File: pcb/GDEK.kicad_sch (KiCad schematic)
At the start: 264 parts, among them J1 TYPE-C-31-M-13C, J101 TYPE-C-31-M-13C, J102 AudioJack3, J103 Debug pads, J2 AudioJack3, J3 Debug pads, SW1 SW_Push_45deg, SW10 SW_Push_45deg, SW101 SW_Push_45deg, SW102 SW_Push_45deg, SW103 SW_Push_45deg, SW104 SW_Push_45deg, SW105 SW_Push_45deg, SW106 SW_Push_45deg, SW107 SW_Push_45deg, SW108 SW_Push_45deg, SW109 SW_Push_45deg, SW11 SW_Push_45deg, SW110 SW_Push_45deg, SW111 SW_Push_45deg, SW112 SW_Push_45deg, SW113 SW_Push_45deg, SW114 SW_Push_45deg, SW115 SW_Push_45deg, SW116 SW_Push_45deg, SW117 SW_Push_45deg, SW118 SW_Push_45deg, SW119 SW_Push_45deg, SW12 SW_Push_45deg, SW120 SW_Push_45deg, SW121 SW_Push_45deg, SW122 SW_Push_45deg, SW123 SW_Push_45deg, SW124 SW_Push_45deg, SW125 SW_Push_45deg, SW126 SW_Push_45deg, SW127 SW_Push_45deg, SW128 SW_Push_45deg, SW129 SW_Push_45deg, SW13 SW_Push_45deg, SW130 SW_Push_45deg, SW131 RotaryEncoder_Switch, SW14 SW_Push_45deg, SW15 SW_Push_45deg, SW16 SW_Push_45deg, SW17 SW_Push_45deg, SW18 SW_Push_45deg, SW19 SW_Push_45deg, SW2 SW_Push_45deg, SW20 SW_Push_45deg, SW21 SW_Push_45deg, SW22 SW_Push_45deg, SW23 SW_Push_45deg, SW24 SW_Push_45deg, SW25 SW_Push_45deg, SW26 SW_Push_45deg, SW27 SW_Push_45deg, SW28 SW_Push_45deg, SW29 SW_Push_45deg, SW3 SW_Push_45deg, SW30 SW_Push_45deg, SW31 RotaryEncoder_Switch, SW4 SW_Push_45deg, SW5 SW_Push_45deg, SW6 SW_Push_45deg, SW7 SW_Push_45deg, SW8 SW_Push_45deg, SW9 SW_Push_45deg, U1 RP2040, U101 RP2040, U102 W25Q128JVP, U103 74AHCT1G125, U104 USBLC6-2P6, U105 XC6210B332MR, U2 W25Q128JVP, U3 74AHCT1G125, U4 USBLC6-2P6, U5 XC6210B332MR, Y1 ABM8-272-T3, Y101 ABM8-272-T3

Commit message: ♻️ Make switch symbol multi-unit for switch and LED
Also changes VBUS_PRESENCE voltage divider’s resistors and handedness pull-up/down resistor in order to remove one reference (10kΩ).
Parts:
- R10, R110: value 10kΩ -> 1kΩ; LCSC C25744 -> C11702
- R102, R2: value 10kΩ -> 5.1kΩ; LCSC C25744 -> C25905
- R11, R111: value 5.1kΩ -> 470Ω; LCSC C25905 -> C25117
- SW1: renamed from D31; footprint GDEK:SK6812MINIE -> GDEK:MX+KailhChoc+GateronKS+SK6812MINI-E_Tight; symbol LED:SK6812MINI -> GDEK:SW+SK6812MINIE
- SW1, SW10, SW101, SW102, SW103, SW104, SW105, SW106, SW107, SW108, SW109, SW11, SW110, SW111, SW112, SW113, SW114, SW115, SW116, SW117, SW118, SW119, SW12, SW120, SW121, SW122, SW123, SW124, SW125, SW126, SW127, SW128, SW129, SW13, SW130, SW14, SW15, SW16, SW17, SW18, SW19, SW2, SW20, SW21, SW22, SW23, SW24, SW25, SW26, SW27, SW28, SW29, SW3, SW30, SW4, SW5, SW6, SW7, SW8, SW9: value SW_Push_45deg -> SK6812MINI; footprint (none) -> GDEK:MX+KailhChoc+GateronKS+SK6812MINI-E_Tight; symbol Switch:SW_Push_45deg -> GDEK:SW+SK6812MINIE; LCSC (none) -> C5149201
- SW10: renamed from D40; footprint GDEK:SK6812MINIE -> GDEK:MX+KailhChoc+GateronKS+SK6812MINI-E_Tight; symbol LED:SK6812MINI -> GDEK:SW+SK6812MINIE
- SW101: renamed from D131; footprint GDEK:SK6812MINIE -> GDEK:MX+KailhChoc+GateronKS+SK6812MINI-E_Tight; symbol LED:SK6812MINI -> GDEK:SW+SK6812MINIE
- SW102: renamed from D132; footprint GDEK:SK6812MINIE -> GDEK:MX+KailhChoc+GateronKS+SK6812MINI-E_Tight; symbol LED:SK6812MINI -> GDEK:SW+SK6812MINIE
- SW103: renamed from D133; footprint GDEK:SK6812MINIE -> GDEK:MX+KailhChoc+GateronKS+SK6812MINI-E_Tight; symbol LED:SK6812MINI -> GDEK:SW+SK6812MINIE
- SW104: renamed from D134; footprint GDEK:SK6812MINIE -> GDEK:MX+KailhChoc+GateronKS+SK6812MINI-E_Tight; symbol LED:SK6812MINI -> GDEK:SW+SK6812MINIE
- SW105: renamed from D135; footprint GDEK:SK6812MINIE -> GDEK:MX+KailhChoc+GateronKS+SK6812MINI-E_Tight; symbol LED:SK6812MINI -> GDEK:SW+SK6812MINIE
- SW106: renamed from D136; footprint GDEK:SK6812MINIE -> GDEK:MX+KailhChoc+GateronKS+SK6812MINI-E_Tight; symbol LED:SK6812MINI -> GDEK:SW+SK6812MINIE
- SW107: renamed from D137; footprint GDEK:SK6812MINIE -> GDEK:MX+KailhChoc+GateronKS+SK6812MINI-E_Tight; symbol LED:SK6812MINI -> GDEK:SW+SK6812MINIE
- SW108: renamed from D138; footprint GDEK:SK6812MINIE -> GDEK:MX+KailhChoc+GateronKS+SK6812MINI-E_Tight; symbol LED:SK6812MINI -> GDEK:SW+SK6812MINIE
- SW109: renamed from D139; footprint GDEK:SK6812MINIE -> GDEK:MX+KailhChoc+GateronKS+SK6812MINI-E_Tight; symbol LED:SK6812MINI -> GDEK:SW+SK6812MINIE
- SW11: renamed from D41; footprint GDEK:SK6812MINIE -> GDEK:MX+KailhChoc+GateronKS+SK6812MINI-E_Tight; symbol LED:SK6812MINI -> GDEK:SW+SK6812MINIE
- SW110: renamed from D140; footprint GDEK:SK6812MINIE -> GDEK:MX+KailhChoc+GateronKS+SK6812MINI-E_Tight; symbol LED:SK6812MINI -> GDEK:SW+SK6812MINIE
- SW111: renamed from D141; footprint GDEK:SK6812MINIE -> GDEK:MX+KailhChoc+GateronKS+SK6812MINI-E_Tight; symbol LED:SK6812MINI -> GDEK:SW+SK6812MINIE
- SW112: renamed from D142; footprint GDEK:SK6812MINIE -> GDEK:MX+KailhChoc+GateronKS+SK6812MINI-E_Tight; symbol LED:SK6812MINI -> GDEK:SW+SK6812MINIE
- SW113: renamed from D143; footprint GDEK:SK6812MINIE -> GDEK:MX+KailhChoc+GateronKS+SK6812MINI-E_Tight; symbol LED:SK6812MINI -> GDEK:SW+SK6812MINIE
- SW114: renamed from D144; footprint GDEK:SK6812MINIE -> GDEK:MX+KailhChoc+GateronKS+SK6812MINI-E_Tight; symbol LED:SK6812MINI -> GDEK:SW+SK6812MINIE
- SW115: renamed from D145; footprint GDEK:SK6812MINIE -> GDEK:MX+KailhChoc+GateronKS+SK6812MINI-E_Tight; symbol LED:SK6812MINI -> GDEK:SW+SK6812MINIE
- SW116: renamed from D146; footprint GDEK:SK6812MINIE -> GDEK:MX+KailhChoc+GateronKS+SK6812MINI-E_Tight; symbol LED:SK6812MINI -> GDEK:SW+SK6812MINIE
- SW117: renamed from D147; footprint GDEK:SK6812MINIE -> GDEK:MX+KailhChoc+GateronKS+SK6812MINI-E_Tight; symbol LED:SK6812MINI -> GDEK:SW+SK6812MINIE
- SW118: renamed from D148; footprint GDEK:SK6812MINIE -> GDEK:MX+KailhChoc+GateronKS+SK6812MINI-E_Tight; symbol LED:SK6812MINI -> GDEK:SW+SK6812MINIE
- SW119: renamed from D149; footprint GDEK:SK6812MINIE -> GDEK:MX+KailhChoc+GateronKS+SK6812MINI-E_Tight; symbol LED:SK6812MINI -> GDEK:SW+SK6812MINIE
- SW12: renamed from D42; footprint GDEK:SK6812MINIE -> GDEK:MX+KailhChoc+GateronKS+SK6812MINI-E_Tight; symbol LED:SK6812MINI -> GDEK:SW+SK6812MINIE
- SW120: renamed from D150; footprint GDEK:SK6812MINIE -> GDEK:MX+KailhChoc+GateronKS+SK6812MINI-E_Tight; symbol LED:SK6812MINI -> GDEK:SW+SK6812MINIE
- SW121: renamed from D151; footprint GDEK:SK6812MINIE -> GDEK:MX+KailhChoc+GateronKS+SK6812MINI-E_Tight; symbol LED:SK6812MINI -> GDEK:SW+SK6812MINIE
- SW122: renamed from D152; footprint GDEK:SK6812MINIE -> GDEK:MX+KailhChoc+GateronKS+SK6812MINI-E_Tight; symbol LED:SK6812MINI -> GDEK:SW+SK6812MINIE
- SW123: renamed from D153; footprint GDEK:SK6812MINIE -> GDEK:MX+KailhChoc+GateronKS+SK6812MINI-E_Tight; symbol LED:SK6812MINI -> GDEK:SW+SK6812MINIE
- SW124: renamed from D154; footprint GDEK:SK6812MINIE -> GDEK:MX+KailhChoc+GateronKS+SK6812MINI-E_Tight; symbol LED:SK6812MINI -> GDEK:SW+SK6812MINIE
- SW125: renamed from D155; footprint GDEK:SK6812MINIE -> GDEK:MX+KailhChoc+GateronKS+SK6812MINI-E_Tight; symbol LED:SK6812MINI -> GDEK:SW+SK6812MINIE
- SW126: renamed from D156; footprint GDEK:SK6812MINIE -> GDEK:MX+KailhChoc+GateronKS+SK6812MINI-E_Tight; symbol LED:SK6812MINI -> GDEK:SW+SK6812MINIE
- SW127: renamed from D157; footprint GDEK:SK6812MINIE -> GDEK:MX+KailhChoc+GateronKS+SK6812MINI-E_Tight; symbol LED:SK6812MINI -> GDEK:SW+SK6812MINIE
- SW128: renamed from D158; footprint GDEK:SK6812MINIE -> GDEK:MX+KailhChoc+GateronKS+SK6812MINI-E_Tight; symbol LED:SK6812MINI -> GDEK:SW+SK6812MINIE
- SW129: renamed from D159; footprint GDEK:SK6812MINIE -> GDEK:MX+KailhChoc+GateronKS+SK6812MINI-E_Tight; symbol LED:SK6812MINI -> GDEK:SW+SK6812MINIE
- SW13: renamed from D43; footprint GDEK:SK6812MINIE -> GDEK:MX+KailhChoc+GateronKS+SK6812MINI-E_Tight; symbol LED:SK6812MINI -> GDEK:SW+SK6812MINIE
- SW130: renamed from D160; footprint GDEK:SK6812MINIE -> GDEK:MX+KailhChoc+GateronKS+SK6812MINI-E_Tight; symbol LED:SK6812MINI -> GDEK:SW+SK6812MINIE
- SW14: renamed from D44; footprint GDEK:SK6812MINIE -> GDEK:MX+KailhChoc+GateronKS+SK6812MINI-E_Tight; symbol LED:SK6812MINI -> GDEK:SW+SK6812MINIE
- SW15: renamed from D45; footprint GDEK:SK6812MINIE -> GDEK:MX+KailhChoc+GateronKS+SK6812MINI-E_Tight; symbol LED:SK6812MINI -> GDEK:SW+SK6812MINIE
- SW16: renamed from D46; footprint GDEK:SK6812MINIE -> GDEK:MX+KailhChoc+GateronKS+SK6812MINI-E_Tight; symbol LED:SK6812MINI -> GDEK:SW+SK6812MINIE
- SW17: renamed from D47; footprint GDEK:SK6812MINIE -> GDEK:MX+KailhChoc+GateronKS+SK6812MINI-E_Tight; symbol LED:SK6812MINI -> GDEK:SW+SK6812MINIE
- SW18: renamed from D48; footprint GDEK:SK6812MINIE -> GDEK:MX+KailhChoc+GateronKS+SK6812MINI-E_Tight; symbol LED:SK6812MINI -> GDEK:SW+SK6812MINIE
- SW19: renamed from D49; footprint GDEK:SK6812MINIE -> GDEK:MX+KailhChoc+GateronKS+SK6812MINI-E_Tight; symbol LED:SK6812MINI -> GDEK:SW+SK6812MINIE
- SW2: renamed from D32; footprint GDEK:SK6812MINIE -> GDEK:MX+KailhChoc+GateronKS+SK6812MINI-E_Tight; symbol LED:SK6812MINI -> GDEK:SW+SK6812MINIE
- SW20: renamed from D50; footprint GDEK:SK6812MINIE -> GDEK:MX+KailhChoc+GateronKS+SK6812MINI-E_Tight; symbol LED:SK6812MINI -> GDEK:SW+SK6812MINIE
- SW21: renamed from D51; footprint GDEK:SK6812MINIE -> GDEK:MX+KailhChoc+GateronKS+SK6812MINI-E_Tight; symbol LED:SK6812MINI -> GDEK:SW+SK6812MINIE
- SW22: renamed from D52; footprint GDEK:SK6812MINIE -> GDEK:MX+KailhChoc+GateronKS+SK6812MINI-E_Tight; symbol LED:SK6812MINI -> GDEK:SW+SK6812MINIE
- SW23: renamed from D53; footprint GDEK:SK6812MINIE -> GDEK:MX+KailhChoc+GateronKS+SK6812MINI-E_Tight; symbol LED:SK6812MINI -> GDEK:SW+SK6812MINIE
- SW24: renamed from D54; footprint GDEK:SK6812MINIE -> GDEK:MX+KailhChoc+GateronKS+SK6812MINI-E_Tight; symbol LED:SK6812MINI -> GDEK:SW+SK6812MINIE
- SW25: renamed from D55; footprint GDEK:SK6812MINIE -> GDEK:MX+KailhChoc+GateronKS+SK6812MINI-E_Tight; symbol LED:SK6812MINI -> GDEK:SW+SK6812MINIE
- SW26: renamed from D56; footprint GDEK:SK6812MINIE -> GDEK:MX+KailhChoc+GateronKS+SK6812MINI-E_Tight; symbol LED:SK6812MINI -> GDEK:SW+SK6812MINIE
- SW27: renamed from D57; footprint GDEK:SK6812MINIE -> GDEK:MX+KailhChoc+GateronKS+SK6812MINI-E_Tight; symbol LED:SK6812MINI -> GDEK:SW+SK6812MINIE
- SW28: renamed from D58; footprint GDEK:SK6812MINIE -> GDEK:MX+KailhChoc+GateronKS+SK6812MINI-E_Tight; symbol LED:SK6812MINI -> GDEK:SW+SK6812MINIE
- SW29: renamed from D59; footprint GDEK:SK6812MINIE -> GDEK:MX+KailhChoc+GateronKS+SK6812MINI-E_Tight; symbol LED:SK6812MINI -> GDEK:SW+SK6812MINIE
- SW3: renamed from D33; footprint GDEK:SK6812MINIE -> GDEK:MX+KailhChoc+GateronKS+SK6812MINI-E_Tight; symbol LED:SK6812MINI -> GDEK:SW+SK6812MINIE
- SW30: renamed from D60; footprint GDEK:SK6812MINIE -> GDEK:MX+KailhChoc+GateronKS+SK6812MINI-E_Tight; symbol LED:SK6812MINI -> GDEK:SW+SK6812MINIE
- SW4: renamed from D34; footprint GDEK:SK6812MINIE -> GDEK:MX+KailhChoc+GateronKS+SK6812MINI-E_Tight; symbol LED:SK6812MINI -> GDEK:SW+SK6812MINIE
- SW5: renamed from D35; footprint GDEK:SK6812MINIE -> GDEK:MX+KailhChoc+GateronKS+SK6812MINI-E_Tight; symbol LED:SK6812MINI -> GDEK:SW+SK6812MINIE
- SW6: renamed from D36; footprint GDEK:SK6812MINIE -> GDEK:MX+KailhChoc+GateronKS+SK6812MINI-E_Tight; symbol LED:SK6812MINI -> GDEK:SW+SK6812MINIE
- SW7: renamed from D37; footprint GDEK:SK6812MINIE -> GDEK:MX+KailhChoc+GateronKS+SK6812MINI-E_Tight; symbol LED:SK6812MINI -> GDEK:SW+SK6812MINIE
- SW8: renamed from D38; footprint GDEK:SK6812MINIE -> GDEK:MX+KailhChoc+GateronKS+SK6812MINI-E_Tight; symbol LED:SK6812MINI -> GDEK:SW+SK6812MINIE
- SW9: renamed from D39; footprint GDEK:SK6812MINIE -> GDEK:MX+KailhChoc+GateronKS+SK6812MINI-E_Tight; symbol LED:SK6812MINI -> GDEK:SW+SK6812MINIE
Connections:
- net +5V: now also SW1.3 (VDD), SW10.3 (VDD), SW11.3 (VDD), SW12.3 (VDD), SW13.3 (VDD), SW14.3 (VDD), SW15.3 (VDD), SW16.3 (VDD), SW17.3 (VDD), SW18.3 (VDD), SW19.3 (VDD), SW2.3 (VDD), SW20.3 (VDD), SW21.3 (VDD), SW22.3 (VDD), SW23.3 (VDD), SW24.3 (VDD), SW25.3 (VDD), SW26.3 (VDD), SW27.3 (VDD), SW28.3 (VDD), SW29.3 (VDD), SW3.3 (VDD), SW30.3 (VDD), SW4.3 (VDD), SW5.3 (VDD), SW6.3 (VDD), SW7.3 (VDD), SW8.3 (VDD), SW9.3 (VDD); no longer SW1.4 (VDD), SW10.4 (VDD), SW11.4 (VDD), SW12.4 (VDD), SW13.4 (VDD), SW14.4 (VDD), SW15.4 (VDD), SW16.4 (VDD), SW17.4 (VDD), SW18.4 (VDD), SW19.4 (VDD), SW2.4 (VDD), SW20.4 (VDD), SW21.4 (VDD), SW22.4 (VDD), SW23.4 (VDD), SW24.4 (VDD), SW25.4 (VDD), SW26.4 (VDD), SW27.4 (VDD), SW28.4 (VDD), SW29.4 (VDD), SW3.4 (VDD), SW30.4 (VDD), SW4.4 (VDD), SW5.4 (VDD), SW6.4 (VDD), SW7.4 (VDD), SW8.4 (VDD), SW9.4 (VDD)
- net +5V_R: now also SW101.3 (VDD), SW102.3 (VDD), SW103.3 (VDD), SW104.3 (VDD), SW105.3 (VDD), SW106.3 (VDD), SW107.3 (VDD), SW108.3 (VDD), SW109.3 (VDD), SW110.3 (VDD), SW111.3 (VDD), SW112.3 (VDD), SW113.3 (VDD), SW114.3 (VDD), SW115.3 (VDD), SW116.3 (VDD), SW117.3 (VDD), SW118.3 (VDD), SW119.3 (VDD), SW120.3 (VDD), SW121.3 (VDD), SW122.3 (VDD), SW123.3 (VDD), SW124.3 (VDD), SW125.3 (VDD), SW126.3 (VDD), SW127.3 (VDD), SW128.3 (VDD), SW129.3 (VDD), SW130.3 (VDD); no longer SW101.4 (VDD), SW102.4 (VDD), SW103.4 (VDD), SW104.4 (VDD), SW105.4 (VDD), SW106.4 (VDD), SW107.4 (VDD), SW108.4 (VDD), SW109.4 (VDD), SW110.4 (VDD), SW111.4 (VDD), SW112.4 (VDD), SW113.4 (VDD), SW114.4 (VDD), SW115.4 (VDD), SW116.4 (VDD), SW117.4 (VDD), SW118.4 (VDD), SW119.4 (VDD), SW120.4 (VDD), SW121.4 (VDD), SW122.4 (VDD), SW123.4 (VDD), SW124.4 (VDD), SW125.4 (VDD), SW126.4 (VDD), SW127.4 (VDD), SW128.4 (VDD), SW129.4 (VDD), SW130.4 (VDD)
- net COL0: now also SW1.5, SW13.5, SW19.5, SW25.5, SW7.5; no longer SW1.1, SW13.1, SW19.1, SW25.1, SW7.1
- net COL0_R: now also SW101.5, SW107.5, SW113.5, SW119.5, SW125.5; no longer SW101.1, SW107.1, SW113.1, SW119.1, SW125.1
- net COL1: now also SW14.5, SW2.5, SW20.5, SW26.5, SW8.5; no longer SW14.1, SW2.1, SW20.1, SW26.1, SW8.1
- net COL1_R: now also SW102.5, SW108.5, SW114.5, SW120.5, SW126.5; no longer SW102.1, SW108.1, SW114.1, SW120.1, SW126.1
- net COL2: now also SW15.5, SW21.5, SW27.5, SW3.5, SW9.5; no longer SW15.1, SW21.1, SW27.1, SW3.1, SW9.1
- net COL2_R: now also SW103.5, SW109.5, SW115.5, SW121.5, SW127.5; no longer SW103.1, SW109.1, SW115.1, SW121.1, SW127.1
- net COL3: now also SW10.5, SW16.5, SW22.5, SW28.5, SW4.5; no longer SW10.1, SW16.1, SW22.1, SW28.1, SW4.1
- net COL3_R: now also SW104.5, SW110.5, SW116.5, SW122.5, SW128.5; no longer SW104.1, SW110.1, SW116.1, SW122.1, SW128.1
- net COL4: now also SW11.5, SW17.5, SW23.5, SW29.5, SW5.5; no longer SW11.1, SW17.1, SW23.1, SW29.1, SW5.1
- net COL4_R: now also SW105.5, SW111.5, SW117.5, SW123.5, SW129.5; no longer SW105.1, SW111.1, SW117.1, SW123.1, SW129.1
- net COL5: now also SW12.5, SW18.5, SW24.5, SW30.5, SW6.5; no longer SW12.1, SW18.1, SW24.1, SW30.1, SW6.1
- net COL5_R: now also SW106.5, SW112.5, SW118.5, SW124.5, SW130.5; no longer SW106.1, SW112.1, SW118.1, SW124.1, SW130.1
- net GND: now also SW1.1 (VSS), SW10.1 (VSS), SW11.1 (VSS), SW12.1 (VSS), SW13.1 (VSS), SW14.1 (VSS), SW15.1 (VSS), SW16.1 (VSS), SW17.1 (VSS), SW18.1 (VSS), SW19.1 (VSS), SW2.1 (VSS), SW20.1 (VSS), SW21.1 (VSS), SW22.1 (VSS), SW23.1 (VSS), SW24.1 (VSS), SW25.1 (VSS), SW26.1 (VSS), SW27.1 (VSS), SW28.1 (VSS), SW29.1 (VSS), SW3.1 (VSS), SW30.1 (VSS), SW4.1 (VSS), SW5.1 (VSS), SW6.1 (VSS), SW7.1 (VSS), SW8.1 (VSS), SW9.1 (VSS); no longer SW1.2 (VSS), SW10.2 (VSS), SW11.2 (VSS), SW12.2 (VSS), SW13.2 (VSS), SW14.2 (VSS), SW15.2 (VSS), SW16.2 (VSS), SW17.2 (VSS), SW18.2 (VSS), SW19.2 (VSS), SW2.2 (VSS), SW20.2 (VSS), SW21.2 (VSS), SW22.2 (VSS), SW23.2 (VSS), SW24.2 (VSS), SW25.2 (VSS), SW26.2 (VSS), SW27.2 (VSS), SW28.2 (VSS), SW29.2 (VSS), SW3.2 (VSS), SW30.2 (VSS), SW4.2 (VSS), SW5.2 (VSS), SW6.2 (VSS), SW7.2 (VSS), SW8.2 (VSS), SW9.2 (VSS)
- net GND_R: now also SW101.1 (VSS), SW102.1 (VSS), SW103.1 (VSS), SW104.1 (VSS), SW105.1 (VSS), SW106.1 (VSS), SW107.1 (VSS), SW108.1 (VSS), SW109.1 (VSS), SW110.1 (VSS), SW111.1 (VSS), SW112.1 (VSS), SW113.1 (VSS), SW114.1 (VSS), SW115.1 (VSS), SW116.1 (VSS), SW117.1 (VSS), SW118.1 (VSS), SW119.1 (VSS), SW120.1 (VSS), SW121.1 (VSS), SW122.1 (VSS), SW123.1 (VSS), SW124.1 (VSS), SW125.1 (VSS), SW126.1 (VSS), SW127.1 (VSS), SW128.1 (VSS), SW129.1 (VSS), SW130.1 (VSS); no longer SW101.2 (VSS), SW102.2 (VSS), SW103.2 (VSS), SW104.2 (VSS), SW105.2 (VSS), SW106.2 (VSS), SW107.2 (VSS), SW108.2 (VSS), SW109.2 (VSS), SW110.2 (VSS), SW111.2 (VSS), SW112.2 (VSS), SW113.2 (VSS), SW114.2 (VSS), SW115.2 (VSS), SW116.2 (VSS), SW117.2 (VSS), SW118.2 (VSS), SW119.2 (VSS), SW120.2 (VSS), SW121.2 (VSS), SW122.2 (VSS), SW123.2 (VSS), SW124.2 (VSS), SW125.2 (VSS), SW126.2 (VSS), SW127.2 (VSS), SW128.2 (VSS), SW129.2 (VSS), SW130.2 (VSS)
- net at D30.2 (A): now also SW30.6; no longer SW30.2
- net at D120.2 (A): now also SW120.6; no longer SW120.2
- net at D17.2 (A): now also SW17.6; no longer SW17.2
- net at D110.2 (A): now also SW110.6; no longer SW110.2
- net at D121.2 (A): now also SW121.6; no longer SW121.2
- net at D29.2 (A): now also SW29.6; no longer SW29.2
- net at D10.2 (A): now also SW10.6; no longer SW10.2
- net at D128.2 (A): now also SW128.6; no longer SW128.2
- net at D16.2 (A): now also SW16.6; no longer SW16.2
- net at D126.2 (A): now also SW126.6; no longer SW126.2
- net at U103.4: now also SW101.2 (DIN); no longer SW101.3 (DIN)
- net at D14.2 (A): now also SW14.6; no longer SW14.2
- net at D23.2 (A): now also SW23.6; no longer SW23.2
- net at D9.2 (A): now also SW9.6; no longer SW9.2
- net at D25.2 (A): now also SW25.6; no longer SW25.2
- net at D115.2 (A): now also SW115.6; no longer SW115.2
- net at D4.2 (A): now also SW4.6; no longer SW4.2
- net at D124.2 (A): now also SW124.6; no longer SW124.2
- net at D20.2 (A): now also SW20.6; no longer SW20.2
- net at D7.2 (A): now also SW7.6; no longer SW7.2
- net at D22.2 (A): now also SW22.6; no longer SW22.2
- net at D18.2 (A): now also SW18.6; no longer SW18.2
- net at D101.2 (A): now also SW101.6; no longer SW101.2
- net at D15.2 (A): now also SW15.6; no longer SW15.2
- net at D2.2 (A): now also SW2.6; no longer SW2.2
- net at D109.2 (A): now also SW109.6; no longer SW109.2
- net at D127.2 (A): now also SW127.6; no longer SW127.2
- net at D13.2 (A): now also SW13.6; no longer SW13.2
- net at D26.2 (A): now also SW26.6; no longer SW26.2
- net at D21.2 (A): now also SW21.6; no longer SW21.2
- net at D106.2 (A): now also SW106.6; no longer SW106.2
- net at D122.2 (A): now also SW122.6; no longer SW122.2
- net at D3.2 (A): now also SW3.6; no longer SW3.2
- net at D117.2 (A): now also SW117.6; no longer SW117.2
- net at D130.2 (A): now also SW130.6; no longer SW130.2
- net at D107.2 (A): now also SW107.6; no longer SW107.2
- net at D119.2 (A): now also SW119.6; no longer SW119.2
- net at D28.2 (A): now also SW28.6; no longer SW28.2
- net at D8.2 (A): now also SW8.6; no longer SW8.2
- net at D11.2 (A): now also SW11.6; no longer SW11.2
- net at D5.2 (A): now also SW5.6; no longer SW5.2
- net at D102.2 (A): now also SW102.6; no longer SW102.2
- net at D24.2 (A): now also SW24.6; no longer SW24.2
- net at D118.2 (A): now also SW118.6; no longer SW118.2
- net at D104.2 (A): now also SW104.6; no longer SW104.2
- net at D129.2 (A): now also SW129.6; no longer SW129.2
- net at D12.2 (A): now also SW12.6; no longer SW12.2
- net at D6.2 (A): now also SW6.6; no longer SW6.2
- net at U3.4: now also SW1.2 (DIN); no longer SW1.3 (DIN)
- net at D108.2 (A): now also SW108.6; no longer SW108.2
- net at D27.2 (A): now also SW27.6; no longer SW27.2
- net at D103.2 (A): now also SW103.6; no longer SW103.2
- net at D123.2 (A): now also SW123.6; no longer SW123.2
- net at D1.2 (A): now also SW1.6; no longer SW1.2
- net at D113.2 (A): now also SW113.6; no longer SW113.2
- net at D114.2 (A): now also SW114.6; no longer SW114.2
- net at D19.2 (A): now also SW19.6; no longer SW19.2
- net at D105.2 (A): now also SW105.6; no longer SW105.2
- net at D125.2 (A): now also SW125.6; no longer SW125.2
- net at D111.2 (A): now also SW111.6; no longer SW111.2
- net at D116.2 (A): now also SW116.6; no longer SW116.2
- net at D112.2 (A): now also SW112.6; no longer SW112.2
- new net: SW101.4 (DOUT), SW102.2 (DIN)
- new net: SW102.4 (DOUT), SW103.2 (DIN)
- new net: SW16.4 (DOUT), SW17.2 (DIN)
- new net: SW17.4 (DOUT), SW18.2 (DIN)
- new net: SW25.4 (DOUT), SW26.2 (DIN)
- new net: SW26.4 (DOUT), SW27.2 (DIN)
- new net: SW117.4 (DOUT), SW118.2 (DIN)
- new net: SW118.4 (DOUT), SW119.2 (DIN)
- new net: SW27.4 (DOUT), SW28.2 (DIN)
- new net: SW28.4 (DOUT), SW29.2 (DIN)
- new net: SW106.4 (DOUT), SW107.2 (DIN)
- new net: SW107.4 (DOUT), SW108.2 (DIN)
- new net: SW18.4 (DOUT), SW19.2 (DIN)
- new net: SW22.4 (DOUT), SW23.2 (DIN)
- new net: SW23.4 (DOUT), SW24.2 (DIN)
- new net: SW29.4 (DOUT), SW30.2 (DIN)
- new net: SW114.4 (DOUT), SW115.2 (DIN)
- new net: SW115.4 (DOUT), SW116.2 (DIN)
- new net: SW1.4 (DOUT), SW2.2 (DIN)
- new net: SW2.4 (DOUT), SW3.2 (DIN)
- new net: SW108.4 (DOUT), SW109.2 (DIN)
- new net: SW14.4 (DOUT), SW15.2 (DIN)
- new net: SW15.4 (DOUT), SW16.2 (DIN)
- new net: SW12.4 (DOUT), SW13.2 (DIN)
- new net: SW13.4 (DOUT), SW14.2 (DIN)
- new net: SW109.4 (DOUT), SW110.2 (DIN)
- new net: SW110.4 (DOUT), SW111.2 (DIN)
- new net: SW113.4 (DOUT), SW114.2 (DIN)
- new net: SW4.4 (DOUT), SW5.2 (DIN)
- new net: SW5.4 (DOUT), SW6.2 (DIN)
- new net: SW24.4 (DOUT), SW25.2 (DIN)
- new net: SW19.4 (DOUT), SW20.2 (DIN)
- new net: SW20.4 (DOUT), SW21.2 (DIN)
- new net: SW3.4 (DOUT), SW4.2 (DIN)
- new net: SW123.4 (DOUT), SW124.2 (DIN)
- new net: SW124.4 (DOUT), SW125.2 (DIN)
- new net: SW103.4 (DOUT), SW104.2 (DIN)
- new net: SW104.4 (DOUT), SW105.2 (DIN)
- new net: SW119.4 (DOUT), SW120.2 (DIN)
- new net: SW120.4 (DOUT), SW121.2 (DIN)
- new net: SW11.4 (DOUT), SW12.2 (DIN)
- new net: SW125.4 (DOUT), SW126.2 (DIN)
- new net: SW126.4 (DOUT), SW127.2 (DIN)
- new net: SW129.4 (DOUT), SW130.2 (DIN)
- new net: SW116.4 (DOUT), SW117.2 (DIN)
- new net: SW21.4 (DOUT), SW22.2 (DIN)
- new net: SW122.4 (DOUT), SW123.2 (DIN)
- new net: SW7.4 (DOUT), SW8.2 (DIN)
- new net: SW8.4 (DOUT), SW9.2 (DIN)
- new net: SW111.4 (DOUT), SW112.2 (DIN)
- new net: SW127.4 (DOUT), SW128.2 (DIN)
- new net: SW121.4 (DOUT), SW122.2 (DIN)
- new net: SW112.4 (DOUT), SW113.2 (DIN)
- new net: SW10.2 (DIN), SW9.4 (DOUT)
- new net: SW10.4 (DOUT), SW11.2 (DIN)
- new net: SW128.4 (DOUT), SW129.2 (DIN)
- new net: SW6.4 (DOUT), SW7.2 (DIN)
- new net: SW105.4 (DOUT), SW106.2 (DIN)

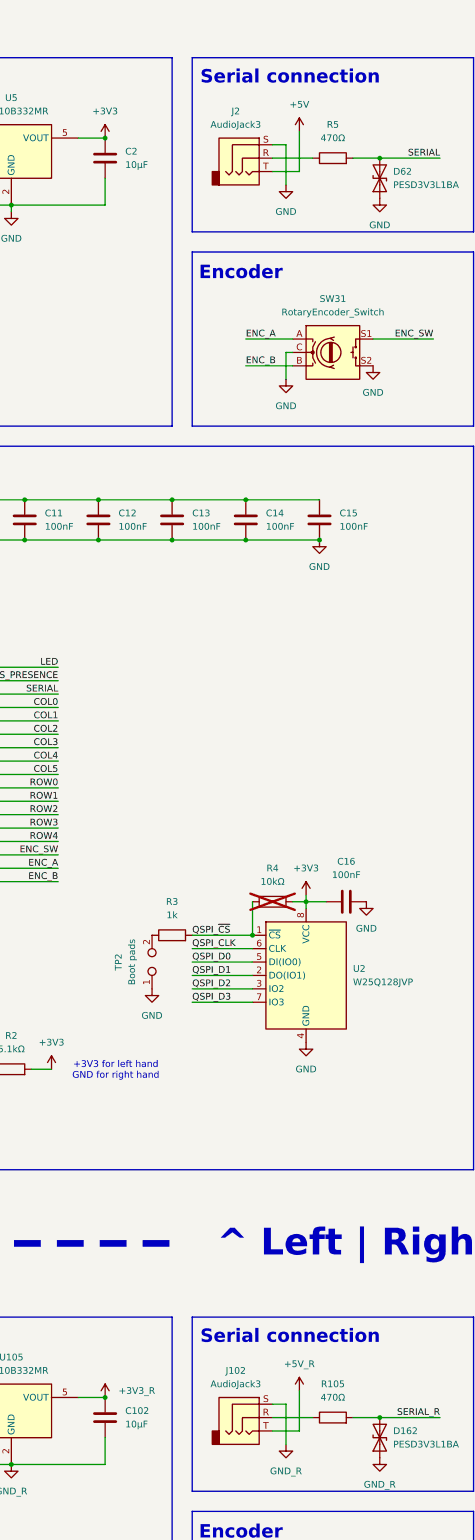
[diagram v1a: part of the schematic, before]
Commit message: 🔧 Finish footprint assignments
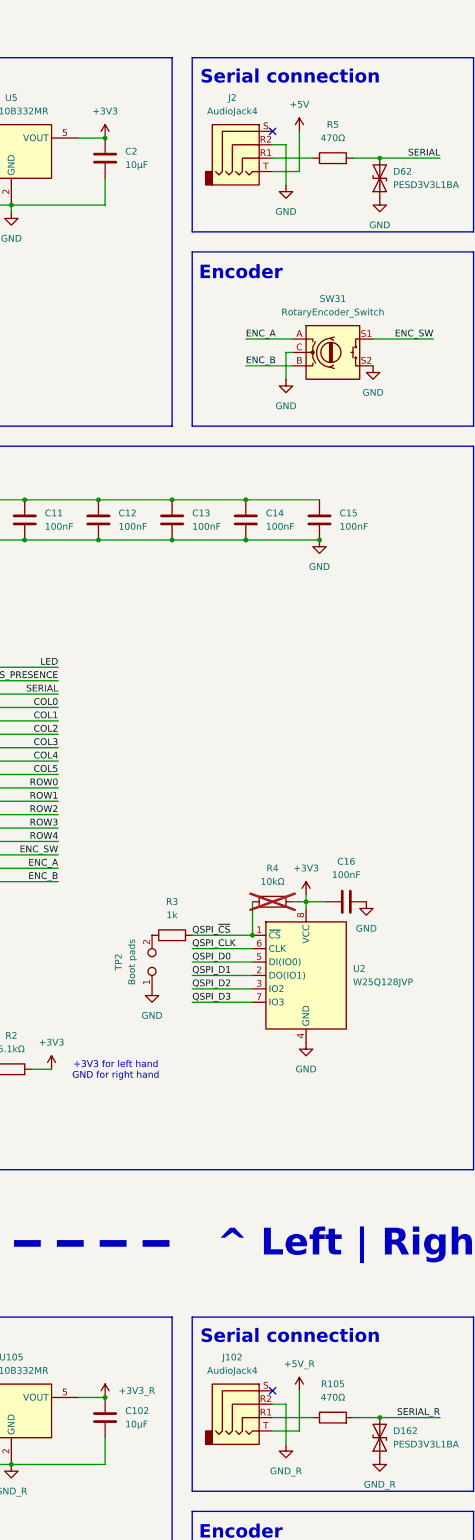
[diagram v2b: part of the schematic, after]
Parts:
- removed J102, J2: AudioJack3, symbol Connector_Audio:AudioJack3
- added J102, J2: AudioJack4, GDEK:AUDIO-TH_PJ-320A-4P-DIP, symbol Connector_Audio:AudioJack4
- SW131, SW31: footprint (none) -> Rotary_Encoder:RotaryEncoder_Alps_EC11E-Switch_Vertical_H20mm
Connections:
- net +5V: now also J2.T
- net +5V_R: now also J102.T
- net GND: now also J2.R2
- net GND_R: now also J102.R2
- net at R5.1: now also J2.R1
- net at R105.1: now also J102.R1
- no-connect marks 30 -> 32
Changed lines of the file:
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@@
 	)
 	(no_connect
+		(at 190.5 274.32)
+	)
+	(no_connect
 		(at 133.35 426.72)
 	)
@@
 	)
 	(no_connect
+		(at 190.5 35.56)
+	)
+	(no_connect
 		(at 133.35 200.66)
 	)
@@
 			)
 		)
-		(property "Footprint" ""
+		(property "Footprint" "Rotary_Encoder:RotaryEncoder_Alps_EC11E-Switch_Vertical_H20mm"
 			(at 198.12 73.406 0)
 			(effects
@@
 	)
 	(symbol
-		(lib_id "Connector_Audio:AudioJack3")
-		(at 185.42 279.4 0)
-		(unit 1)
-		(exclude_from_sim no)
-		(in_bom yes)
-		(on_board yes)
-		(dnp no)
-		(fields_autoplaced yes)
-		(property "Reference" "J102"
-			(at 183.515 270.51 0)
-			(effects
-				(font
-					(size 1.27 1.27)
-				)
-			)
-		)
-		(property "Value" "AudioJack3"
-			(at 183.515 273.05 0)
-			(effects
-				(font
-					(size 1.27 1.27)
-				)
-			)
-		)
-		(property "Footprint" ""
-			(at 185.42 279.4 0)
-			(effects
-				(font
-					(size 1.27 1.27)
-				)
-				(hide yes)
-			)
-		)
-		(property "Datasheet" "~"
-			(at 185.42 279.4 0)
-			(effects
-				(font
-					(size 1.27 1.27)
-				)
-				(hide yes)
-			)
-		)
-		(property "Description" "Audio Jack, 3 Poles (Stereo / TRS)"
-			(at 185.42 279.4 0)
-			(effects
-				(font
-					(size 1.27 1.27)
-				)
-				(hide yes)
-			)
-		)
-		(pin "S"
-		)
-		(pin "T"
-		)
-		(pin "R"
-		)
-		(instances
-			(project "GDEK"
-				(path "/c27e6219-942d-4ad4-b4df-18894276b69d"
-					(reference "J102")
-					(unit 1)
-				)
-			)
-		)
-	)
-	(symbol
 		(lib_id "power:PWR_FLAG")
 		(at -20.32 34.29 180)
@@
 			)
 		)
-		(property "Footprint" ""
+		(property "Footprint" "Rotary_Encoder:RotaryEncoder_Alps_EC11E-Switch_Vertical_H20mm"
 			(at 198.12 312.166 0)
 			(effects
@@
 	)
 	(symbol
+		(lib_id "Connector_Audio:AudioJack4")
+		(at 185.42 276.86 0)
+		(unit 1)
+		(exclude_from_sim no)
+		(in_bom yes)
+		(on_board yes)
+		(dnp no)
+		(fields_autoplaced yes)
+		(property "Reference" "J102"
+			(at 182.88 267.97 0)
+			(effects
+				(font
+					(size 1.27 1.27)
+				)
+			)
+		)
+		(property "Value" "AudioJack4"
+			(at 182.88 270.51 0)
+			(effects
+				(font
+					(size 1.27 1.27)
+				)
+			)
+		)
+		(property "Footprint" "GDEK:AUDIO-TH_PJ-320A-4P-DIP"
+			(at 185.42 276.86 0)
+			(effects
+				(font
+					(size 1.27 1.27)
+				)
+				(hide yes)
+			)
+		)
+		(property "Datasheet" "~"
+			(at 185.42 276.86 0)
+			(effects
+				(font
+					(size 1.27 1.27)
+				)
+				(hide yes)
+			)
+		)
+		(property "Description" "Audio Jack, 4 Poles (TRRS)"
+			(at 185.42 276.86 0)
+			(effects
+				(font
+					(size 1.27 1.27)
+				)
+				(hide yes)
+			)
+		)
+		(property "LCSC" "C18185602"
+			(at 185.42 276.86 0)
+			(effects
+				(font
+					(size 1.27 1.27)
+				)
+				(hide yes)
+			)
+		)
+		(pin "S"
+		)
+		(pin "R1"
+		)
+		(pin "R2"
+		)
+		(pin "T"
+		)
+		(instances
+			(project "GDEK"
+				(path "/c27e6219-942d-4ad4-b4df-18894276b69d"
+					(reference "J102")
+					(unit 1)
+				)
+			)
+		)
+	)
+	(symbol
 		(lib_id "Power_Protection:USBLC6-2P6")
 		(at 81.28 311.15 0)
@@
 	)
 	(symbol
+		(lib_id "Connector_Audio:AudioJack4")
+		(at 185.42 38.1 0)
+		(unit 1)
+		(exclude_from_sim no)
+		(in_bom yes)
+		(on_board yes)
+		(dnp no)
+		(fields_autoplaced yes)
+		(property "Reference" "J2"
+			(at 182.88 29.21 0)
+			(effects
+				(font
+					(size 1.27 1.27)
+				)
+			)
+		)
+		(property "Value" "AudioJack4"
+			(at 182.88 31.75 0)
+			(effects
+				(font
+					(size 1.27 1.27)
+				)
+			)
+		)
+		(property "Footprint" "GDEK:AUDIO-TH_PJ-320A-4P-DIP"
+			(at 185.42 38.1 0)
+			(effects
+				(font
+					(size 1.27 1.27)
+				)
+				(hide yes)
+			)
+		)
+		(property "Datasheet" "~"
+			(at 185.42 38.1 0)
+			(effects
+				(font
+					(size 1.27 1.27)
+				)
+				(hide yes)
+			)
+		)
+		(property "Description" "Audio Jack, 4 Poles (TRRS)"
+			(at 185.42 38.1 0)
+			(effects
+				(font
+					(size 1.27 1.27)
+				)
+				(hide yes)
+			)
+		)
+		(property "LCSC" "C18185602"
+			(at 185.42 38.1 0)
+			(effects
+				(font
+					(size 1.27 1.27)
+				)
+				(hide yes)
+			)
+		)
+		(pin "S"
+		)
+		(pin "R1"
+		)
+		(pin "R2"
+		)
+		(pin "T"
+		)
+		(instances
+			(project ""
+				(path "/c27e6219-942d-4ad4-b4df-18894276b69d"
+					(reference "J2")
+					(unit 1)
+				)
+			)
+		)
+	)
+	(symbol
 		(lib_id "Device:R")
 		(at 78.74 386.08 90)
@@
 					(unit 1)
 				)
-			)
-		)
-	)
-	(symbol
-		(lib_id "Connector_Audio:AudioJack3")
-		(at 185.42 40.64 0)
-		(unit 1)
-		(exclude_from_sim no)
-		(in_bom yes)
-		(on_board yes)
-		(dnp no)
-		(fields_autoplaced yes)
-		(property "Reference" "J2"
-			(at 183.515 31.75 0)
-			(effects
-				(font
-					(size 1.27 1.27)
-				)
-			)
-		)
-		(property "Value" "AudioJack3"
-			(at 183.515 34.29 0)
-			(effects
-				(font
-					(size 1.27 1.27)
-				)
-			)
-		)
-		(property "Footprint" ""
-			(at 185.42 40.64 0)
-			(effects
-				(font
-					(size 1.27 1.27)
-				)
-				(hide yes)
-			)
-		)
-		(property "Datasheet" "~"
-			(at 185.42 40.64 0)
-			(effects
-				(font
-					(size 1.27 1.27)
-				)
-				(hide yes)
-			)
-		)
-		(property "Description" "Audio Jack, 3 Poles (Stereo / TRS)"
-			(at 185.42 40.64 0)
-			(effects
-				(font
-					(size 1.27 1.27)
-				)
-				(hide yes)
-			)
-		)
-		(pin "S"
-		)
-		(pin "T"
-		)
-		(pin "R"
-		)
-		(instances
-			(project ""
-				(path "/c27e6219-942d-4ad4-b4df-18894276b69d"
-					(reference "J2")
-					(unit 1)
-				)

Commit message: ✨ Finish left hand PCB
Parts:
- removed U102, U2: W25Q128JVP, Package_SON:WSON-8-1EP_6x5mm_P1.27mm_EP3.4x4.3mm, symbol Memory_Flash:W25Q128JVP
- added U102, U2: W25Q128JVS, Package_SO:SOIC-8_5.23x5.23mm_P1.27mm, symbol Memory_Flash:W25Q128JVS
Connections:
- net +3V3: now also U2.8 (VCC)
- net +3V3_R: now also U102.8 (VCC)
- net COL0: now also U1.39 (GPIO27_ADC1); no longer U1.5 (GPIO3)
- net COL1: now also U1.38 (GPIO26_ADC0); no longer U1.6 (GPIO4)
- net COL2: now also U1.37 (GPIO25); no longer U1.7 (GPIO5)
- net COL3: now also U1.36 (GPIO24); no longer U1.8 (GPIO6)
- net COL4: now also U1.35 (GPIO23); no longer U1.9 (GPIO7)
- net COL5: now also U1.34 (GPIO22); no longer U1.11 (GPIO8)
- net ENC_A: now also U1.17 (GPIO14); no longer U1.18 (GPIO15)
- net ENC_B: now also U1.18 (GPIO15); no longer U1.27 (GPIO16)
- net ENC_SW: now also U1.16 (GPIO13); no longer U1.17 (GPIO14)
- net GND: now also U2.4 (GND)
- net GND_R: now also U102.4 (GND)
- net LED: now also U1.41 (GPIO29_ADC3); no longer U1.2 (GPIO0)
- net QSPI_CLK: now also U2.6 (CLK)
- net QSPI_CLK_R: now also U102.6 (CLK)
- net QSPI_D0: now also U2.5 (DI(IO0))
- net QSPI_D0_R: now also U102.5 (DI(IO0))
- net QSPI_D1: now also U2.2 (DO(IO1))
- net QSPI_D1_R: now also U102.2 (DO(IO1))
- net QSPI_D2: now also U2.3 (IO2)
- net QSPI_D2_R: now also U102.3 (IO2)
- net QSPI_D3: now also U2.7 (IO3)
- net QSPI_D3_R: now also U102.7 (IO3)
- net QSPI_~{CS}: now also U2.1 (~{CS})
- net QSPI_~{CS}_R: now also U102.1 (~{CS})
- net ROW0: now also U1.40 (GPIO28_ADC2); no longer U1.12 (GPIO9)
- net ROW1: now also U1.32 (GPIO21); no longer U1.13 (GPIO10)
- net ROW2: now also U1.31 (GPIO20); no longer U1.14 (GPIO11)
- net ROW3: now also U1.30 (GPIO19); no longer U1.15 (GPIO12)
- net ROW4: now also U1.29 (GPIO18); no longer U1.16 (GPIO13)
- net SERIAL: now also U1.3 (GPIO1); no longer U1.4 (GPIO2)
- net VBUS_PRESENCE: now also U1.2 (GPIO0); no longer U1.3 (GPIO1)
- net at SW17.2 (DIN): now also SW18.4 (DOUT); no longer SW16.4 (DOUT)
- net at SW17.4 (DOUT): now also SW16.2 (DIN); no longer SW18.2 (DIN)
- net at SW26.2 (DIN): now also SW27.4 (DOUT); no longer SW25.4 (DOUT)
- net at SW26.4 (DOUT): now also SW25.2 (DIN); no longer SW27.2 (DIN)
- net at SW28.2 (DIN): now also SW29.4 (DOUT); no longer SW27.4 (DOUT)
- net at SW28.4 (DOUT): now also SW27.2 (DIN); no longer SW29.2 (DIN)
- net at SW19.2 (DIN): now also SW13.4 (DOUT); no longer SW18.4 (DOUT)
- net at SW30.2 (DIN): now also SW24.4 (DOUT); no longer SW29.4 (DOUT)
- net at SW2.2 (DIN): now also SW3.4 (DOUT); no longer SW1.4 (DOUT)
- net at SW2.4 (DOUT): now also SW1.2 (DIN); no longer SW3.2 (DIN)
- net at SW30.4 (DOUT): now also SW29.2 (DIN)
- net at SW15.2 (DIN): now also SW16.4 (DOUT); no longer SW14.4 (DOUT)
- net at SW15.4 (DOUT): now also SW14.2 (DIN); no longer SW16.2 (DIN)
- net at SW12.4 (DOUT): now also SW18.2 (DIN); no longer SW13.2 (DIN)
- net at SW5.2 (DIN): now also SW6.4 (DOUT); no longer SW4.4 (DOUT)
- net at SW5.4 (DOUT): now also SW4.2 (DIN); no longer SW6.2 (DIN)
- net at R2.1: now also U1.15 (GPIO12); no longer U1.41 (GPIO29_ADC3)
- net at U3.4: now also SW6.2 (DIN); no longer SW1.2 (DIN)
- net at SW7.2 (DIN): now also SW1.4 (DOUT); no longer SW6.4 (DOUT)
- new net: SW13.2 (DIN), SW14.4 (DOUT)
- new net: SW3.2 (DIN), SW4.4 (DOUT)
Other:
- moved on the sheet: F1, R2, R8, R9, SW13B, SW14B, SW15B, SW16B, SW17B, SW18B, SW1B, SW25B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

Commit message: ✨ Add optional decoupling for each LED
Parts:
- added C117, C118, C119, C120, C121, C122, C123, C124, C125, C126, C127, C128, C129, C130, C131, C132, C133, C134, C135, C136, C137, C138, C139, C140, C141, C142, C143, C144, C145, C146, C147, C17, C18, C19, C20, C21, C22, C23, C24, C25, C26, C27, C28, C29, C30, C31, C32, C33, C34, C35, C36, C37, C38, C39, C40, C41, C42, C43, C44, C45, C46, C47: 100nF, Capacitor_SMD:C_0402_1005Metric, symbol Device:C
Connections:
- net +5V: now also C17.2, C18.2, C19.2, C20.2, C21.2, C22.2, C23.2, C24.2, C25.2, C26.2, C27.2, C28.2, C29.2, C30.2, C31.2, C32.2, C33.2, C34.2, C35.2, C36.2, C37.2, C38.2, C39.2, C40.2, C41.2, C42.2, C43.2, C44.2, C45.2, C46.2, C47.2
- net +5V_R: now also C117.2, C118.2, C119.2, C120.2, C121.2, C122.2, C123.2, C124.2, C125.2, C126.2, C127.2, C128.2, C129.2, C130.2, C131.2, C132.2, C133.2, C134.2, C135.2, C136.2, C137.2, C138.2, C139.2, C140.2, C141.2, C142.2, C143.2, C144.2, C145.2, C146.2, C147.2
- net GND: now also C117.1, C17.1, C18.1, C19.1, C20.1, C21.1, C22.1, C23.1, C24.1, C25.1, C26.1, C27.1, C28.1, C29.1, C30.1, C31.1, C32.1, C33.1, C34.1, C35.1, C36.1, C37.1, C38.1, C39.1, C40.1, C41.1, C42.1, C43.1, C44.1, C45.1, C46.1, C47.1
- net GND_R: now also C118.1, C119.1, C120.1, C121.1, C122.1, C123.1, C124.1, C125.1, C126.1, C127.1, C128.1, C129.1, C130.1, C131.1, C132.1, C133.1, C134.1, C135.1, C136.1, C137.1, C138.1, C139.1, C140.1, C141.1, C142.1, C143.1, C144.1, C145.1, C146.1, C147.1
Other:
- note added: "↑ Left | Right ↓"
- note removed: "^ Left | Right v"
- moved on the sheet: C1, C10, C101, C102, C103, C104, C105, C106, C107, C108, C109, C11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
